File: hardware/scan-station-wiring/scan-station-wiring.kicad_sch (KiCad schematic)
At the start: 66 parts, among them J10 Buttons/Encoder, J11 GPIO Expansion, J1A CYD Expansion (SPI2), J1B CYD UART (PWR+HS), J2 NFC Antenna A, J3 RGB LED Header, J4 NFC Antenna B, J5 USB-C, J6 Load Cell, J7 CAN Bus, J8 I2C1 Expansion, J9 TOF Sensor (I2C1), Q1 TVDD_SW_A, Q2 TVDD_SW_B, Q3 BSS138 (SDA), Q4 BSS138 (SCL), SW1 RESET, SW2 BOOT, U1 ESP32-S3-WROOM-1, U2 ADS1220IPWR, U3 AHT20, U4 PN5180A0HN, U5 AS7341-DLGM, U6 AMS1117-3.3, U7 SN65HVD230DR, U8 AMS1117-1.8, Y1 27.12MHz

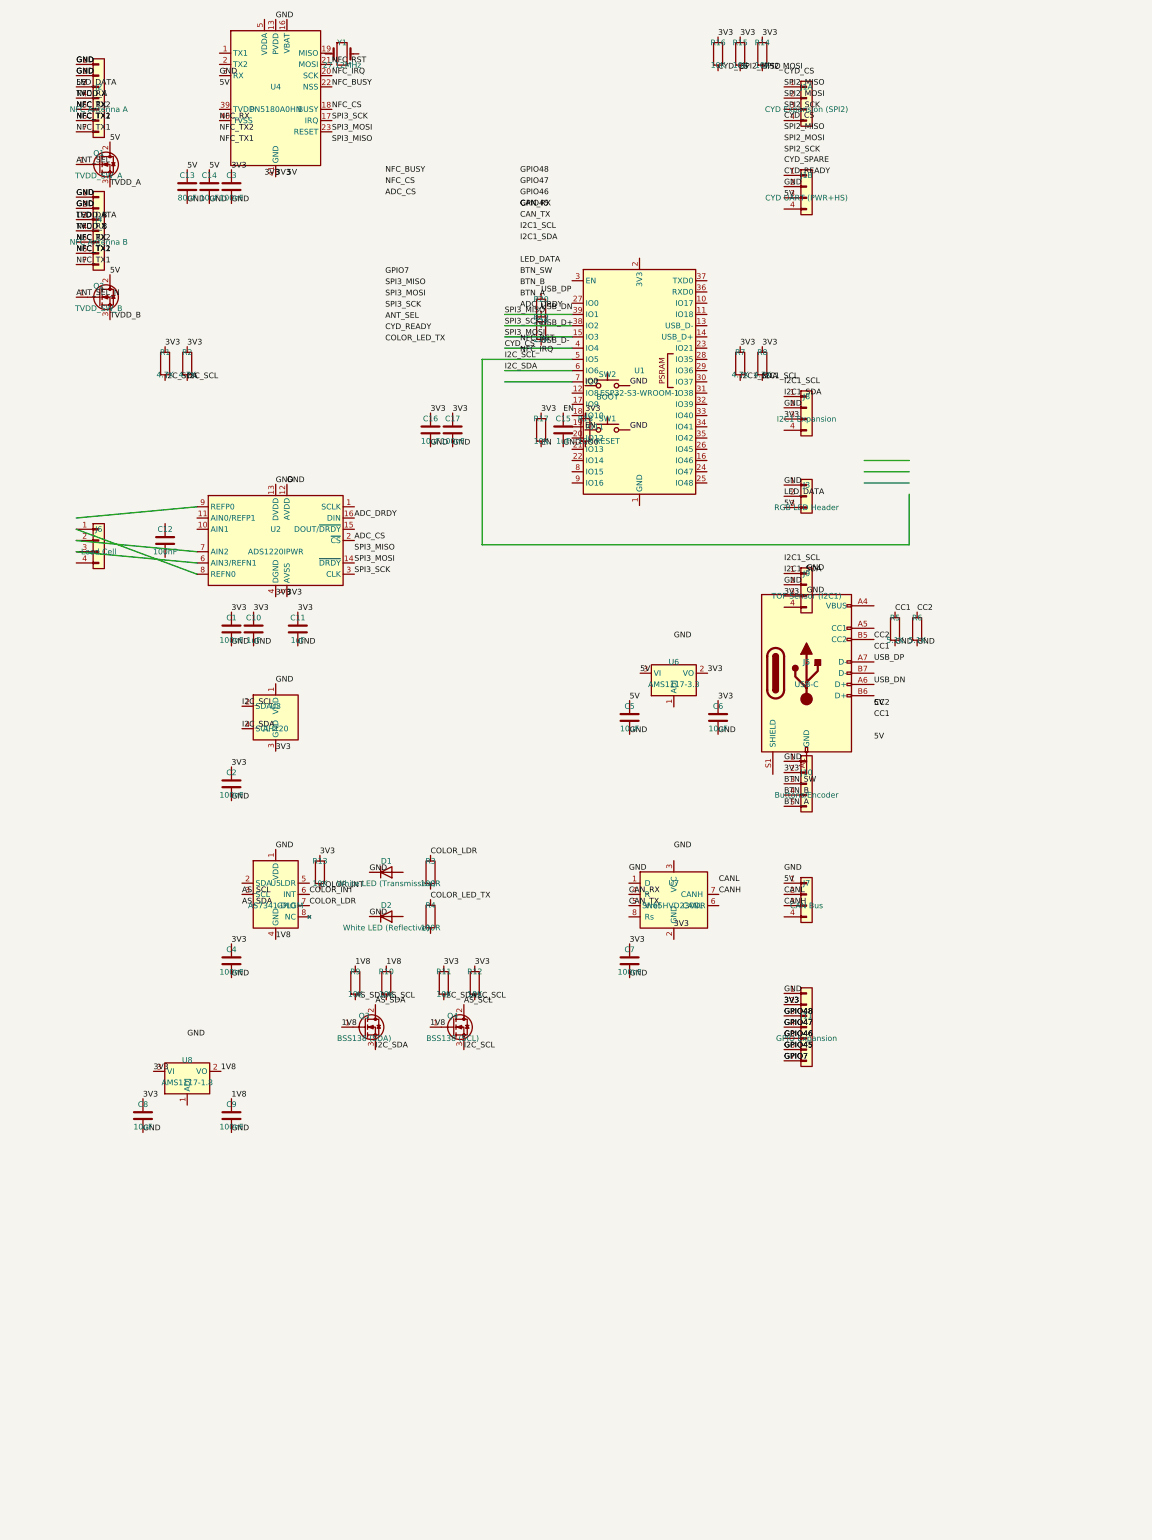
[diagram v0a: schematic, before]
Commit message: feat: add dual USB, CH340C, W5500 Ethernet, PoE header
Major additions:
- CH340C USB-to-UART (U9) for programming via J5 USB-C (IO43/IO44)
- USB OTG host port (J12 USB-C) on IO19/IO20 for label printers
- W5500 Ethernet controller (U10) on SPI3 bus with RJ45 MagJack (J13)
- PoE module headers: J14 (48V input from RJ45) + J15 (5V output)
  Compatible with off-the-shelf PoE PD modules
- Reset button (SW1) + Boot button (SW2) for bare WROOM module
- CYD connector GPIOs corrected (carrier IO7/IO45, not CYD IO43/44)

All 41 ESP32-S3 GPIOs now assigned. Full pin map:
- SPI2 (IO10-13): CYD display
- SPI3 (IO4-6): ADS1220 + PN5180 + W5500
- I2C0 (IO8-9): AHT20 + AS7341
- I2C1 (IO39-40): TOF + expansion
- CAN (IO41-42): SN65HVD230
- UART (IO43-44): CH340C programming
- USB OTG (IO19-20): Host mode
- ETH (IO46-48): W5500 CS/INT/RST
- NFC (IO14-18): PN5180 CS/BUSY/IRQ/RST
- Misc: LED_DATA(38), ANT_SEL(3), buttons(35-37), color(1,7)

Co-Authored-By: Claude Opus 4.6 (1M context) <noreply@anthropic.com>
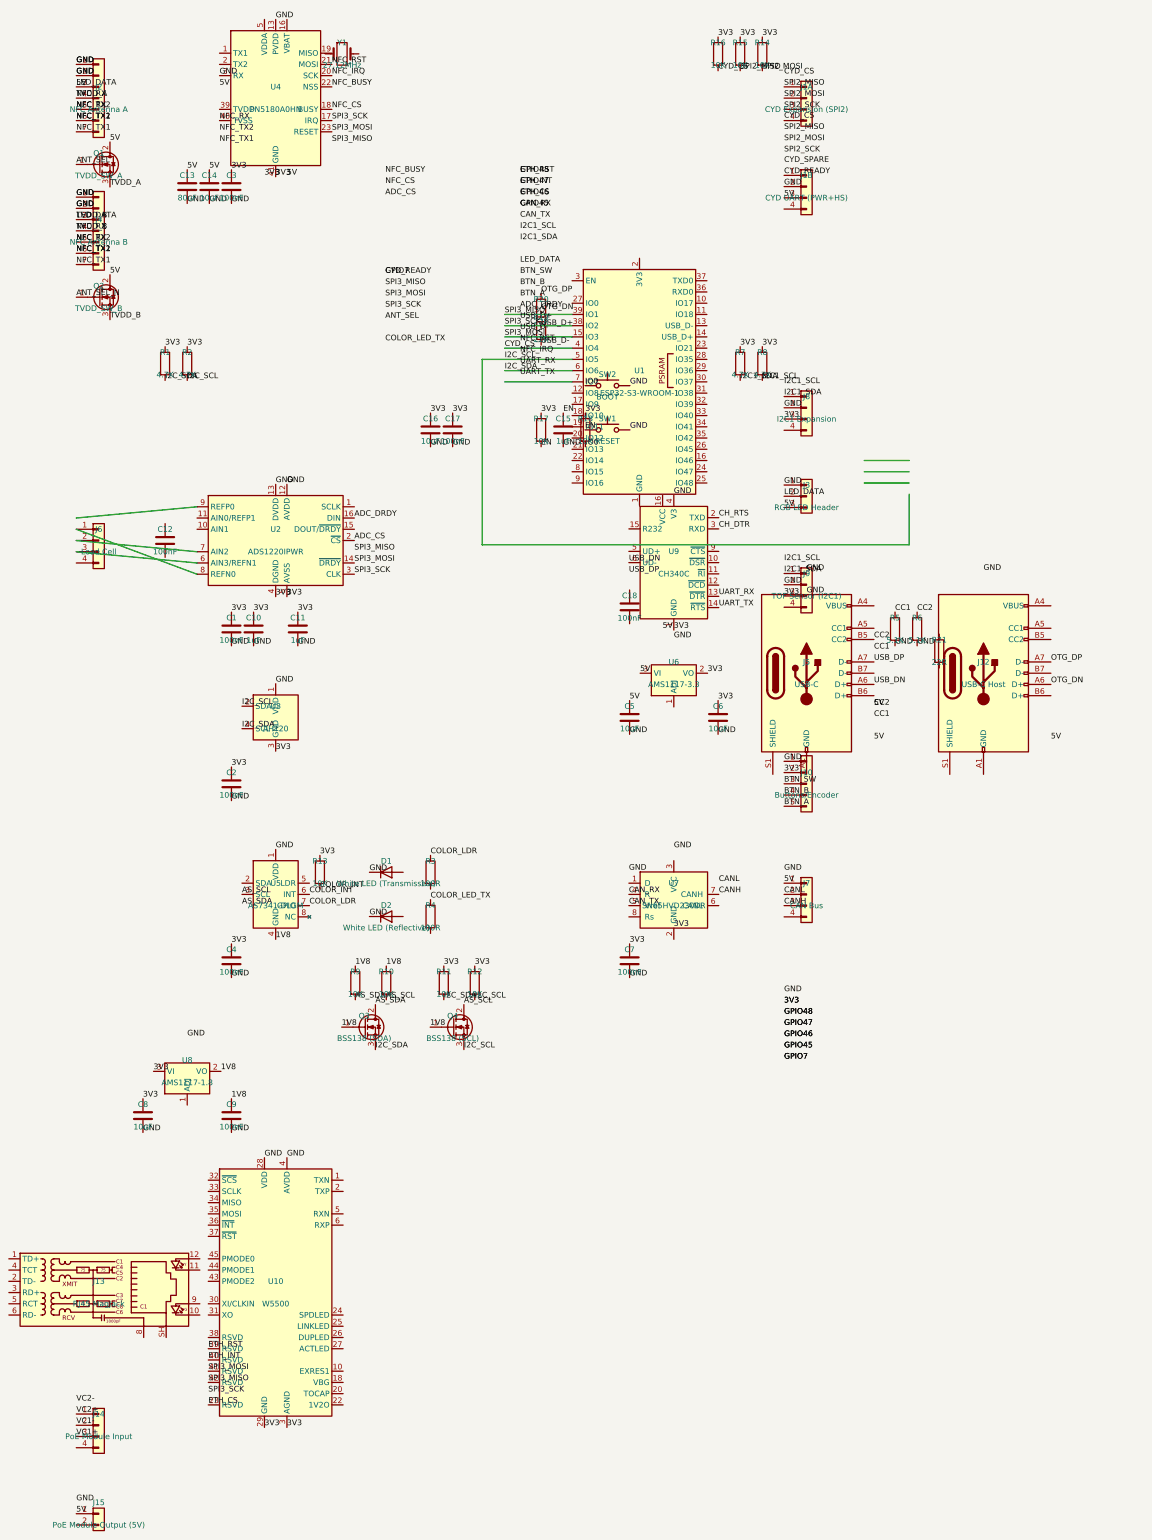
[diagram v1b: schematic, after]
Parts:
- removed J11: GPIO Expansion, symbol Connector_Generic:Conn_01x07
- added C18: 100nF, symbol Device:C
- added J12: USB-C Host, symbol Connector:USB_C_Receptacle_USB2.0_14P
- added J13: RJ45 MagJack, symbol Connector:RJ45_Hanrun_HR911105A_Horizontal
- added J14: PoE Module Input, symbol Connector_Generic:Conn_01x04
- added J15: PoE Module Output (5V), symbol Connector_Generic:Conn_01x02
- added R21: 22R, symbol Device:R
- added U10: W5500, symbol Interface_Ethernet:W5500
- added U9: CH340C, symbol Interface_USB:CH340C
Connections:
- net 3V3: now also U10.14 (AGND), U10.16 (AGND), U10.19 (AGND), U10.29 (GND), U10.3 (AGND), U10.48 (AGND), U10.9 (AGND), U9.1 (GND)
- net 5V: now also J15.1 (Pin_1)
- net GND: now also U10.11 (AVDD), U10.15 (AVDD), U10.17 (AVDD), U10.21 (AVDD), U10.28 (VDD), U10.4 (AVDD), U10.8 (AVDD), U9.4 (V3)
- net SPI3_MISO: now also U10.42 (RSVD)
- net SPI3_MOSI: now also U10.41 (RSVD)
- net USB_DN: now also U9.6 (UD-); no longer R19.1
- net USB_DP: no longer R20.1
- new net: J12.A1 (GND), J12.A12 (GND), J12.B1 (GND), J12.B12 (GND)
- new net: J12.A4 (VBUS), J12.A9 (VBUS), J12.B4 (VBUS), J12.B9 (VBUS)
- new net CH_DTR: U9.3 (RXD)
- new net CH_RTS: U9.2 (TXD)
- new net ETH_CS: U10.23 (RSVD)
- new net ETH_INT: U10.40 (RSVD)
- new net ETH_RST: U10.39 (RSVD)
- new net OTG_DN: J12.A6 (D+), R19.1
- new net OTG_DP: J12.A7 (D-), R20.1
- new net UART_RX: U9.13 (~{DTR})
- new net UART_TX: U9.14 (~{RTS})
- new net VC1+: J14.3 (Pin_3)
- new net VC1-: J14.2 (Pin_2)
- new net VC2+: J14.1 (Pin_1)

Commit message: feat: second load cell, touch buttons, auto-reset, ETH LEDs, PSRAM
- Second load cell connector (J16) on ADS1220 AIN2/AIN3 for FillaShelf
- Move buttons to touch-capable pins (IO1/IO2/IO7 → BTN_SW/A/B)
  Non-touch functions (CYD_READY, CYD_SPARE, COLOR_LED_TX) to IO35-37
- CH340C auto-reset circuit: DTR→EN, RTS→IO0 via 100nF caps (C19/C20)
- W5500 LED outputs wired to RJ45 MagJack (LINKLED, ACTLED)
- W5500 TX/RX pairs connected to RJ45 MagJack
- ESP32-S3-WROOM-1-N16R8 (16MB flash + 8MB PSRAM) specified

Updated GPIO map:
- IO1 → BTN_SW (touch capable)
- IO2 → BTN_A (touch capable)
- IO7 → BTN_B (touch capable)
- IO35 → CYD_READY
- IO36 → CYD_SPARE
- IO37 → COLOR_LED_TX

Co-Authored-By: Claude Opus 4.6 (1M context) <noreply@anthropic.com>
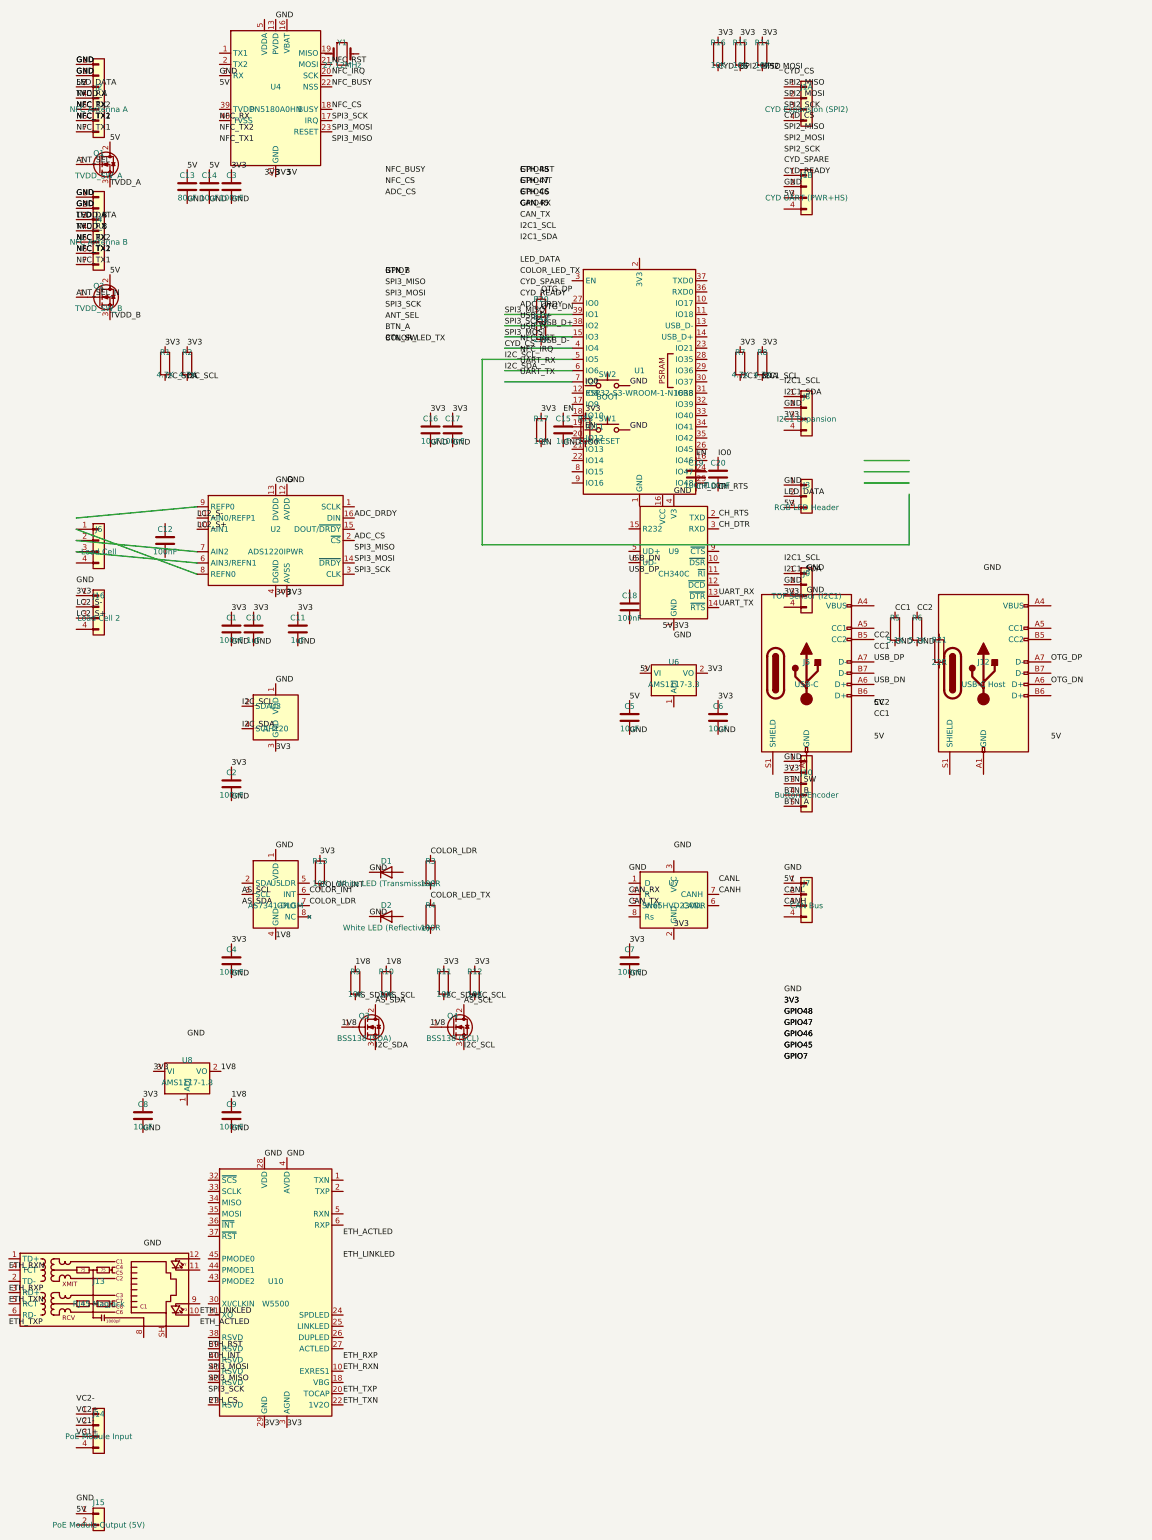
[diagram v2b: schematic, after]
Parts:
- added C19, C20: 100nF, symbol Device:C
- added J16: Load Cell 2, symbol Connector_Generic:Conn_01x04
- U1: value ESP32-S3-WROOM-1 -> ESP32-S3-WROOM-1-N16R8
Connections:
- net COLOR_LED_TX is gone; now on net BTN_SW: R4.1
- net 3V3: now also J16.1 (Pin_1)
- net CH_DTR: now also C19.2
- net CH_RTS: now also C20.2
- net EN: now also C19.1
- net IO0: now also C20.1
- net ETH_RXN: now reaches U10.10 (EXRES1)
- net ETH_RXN: now also J13.4 (TCT)
- net ETH_TXP: now reaches U10.20 (TOCAP)
- net ETH_TXN: now reaches U10.22 (1V2O)
- net ETH_TXN: now also J13.5 (RCT)
- net LC2_S+: now reaches U2.10 (AIN1)
- net LC2_S+: now also J16.3 (Pin_3)
- net LC2_S-: now reaches U2.11 (AIN0/REFP1)
- net LC2_S-: now also J16.2 (Pin_2)
- net ETH_LINKLED: now reaches J13.10
- net ETH_RXP: now reaches J13.3 (RD+)

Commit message: chore: second schematic cleanup pass
- Remove 22 orphaned labels (GPIO expansion, duplicates, stale pins)
- Pretty-print .kicad_sch (was single line again after MCP edits)
- Fix CYD_SPARE label on ESP32 IO36
- Remove old COLOR_LED_TX from IO1 (moved to IO37)
- Remove GPIO7/45/46/47/48 expansion labels (J11 deleted)
- Remove duplicate GND/3V3 labels at old antenna connector positions

Co-Authored-By: Claude Opus 4.6 (1M context) <noreply@anthropic.com>
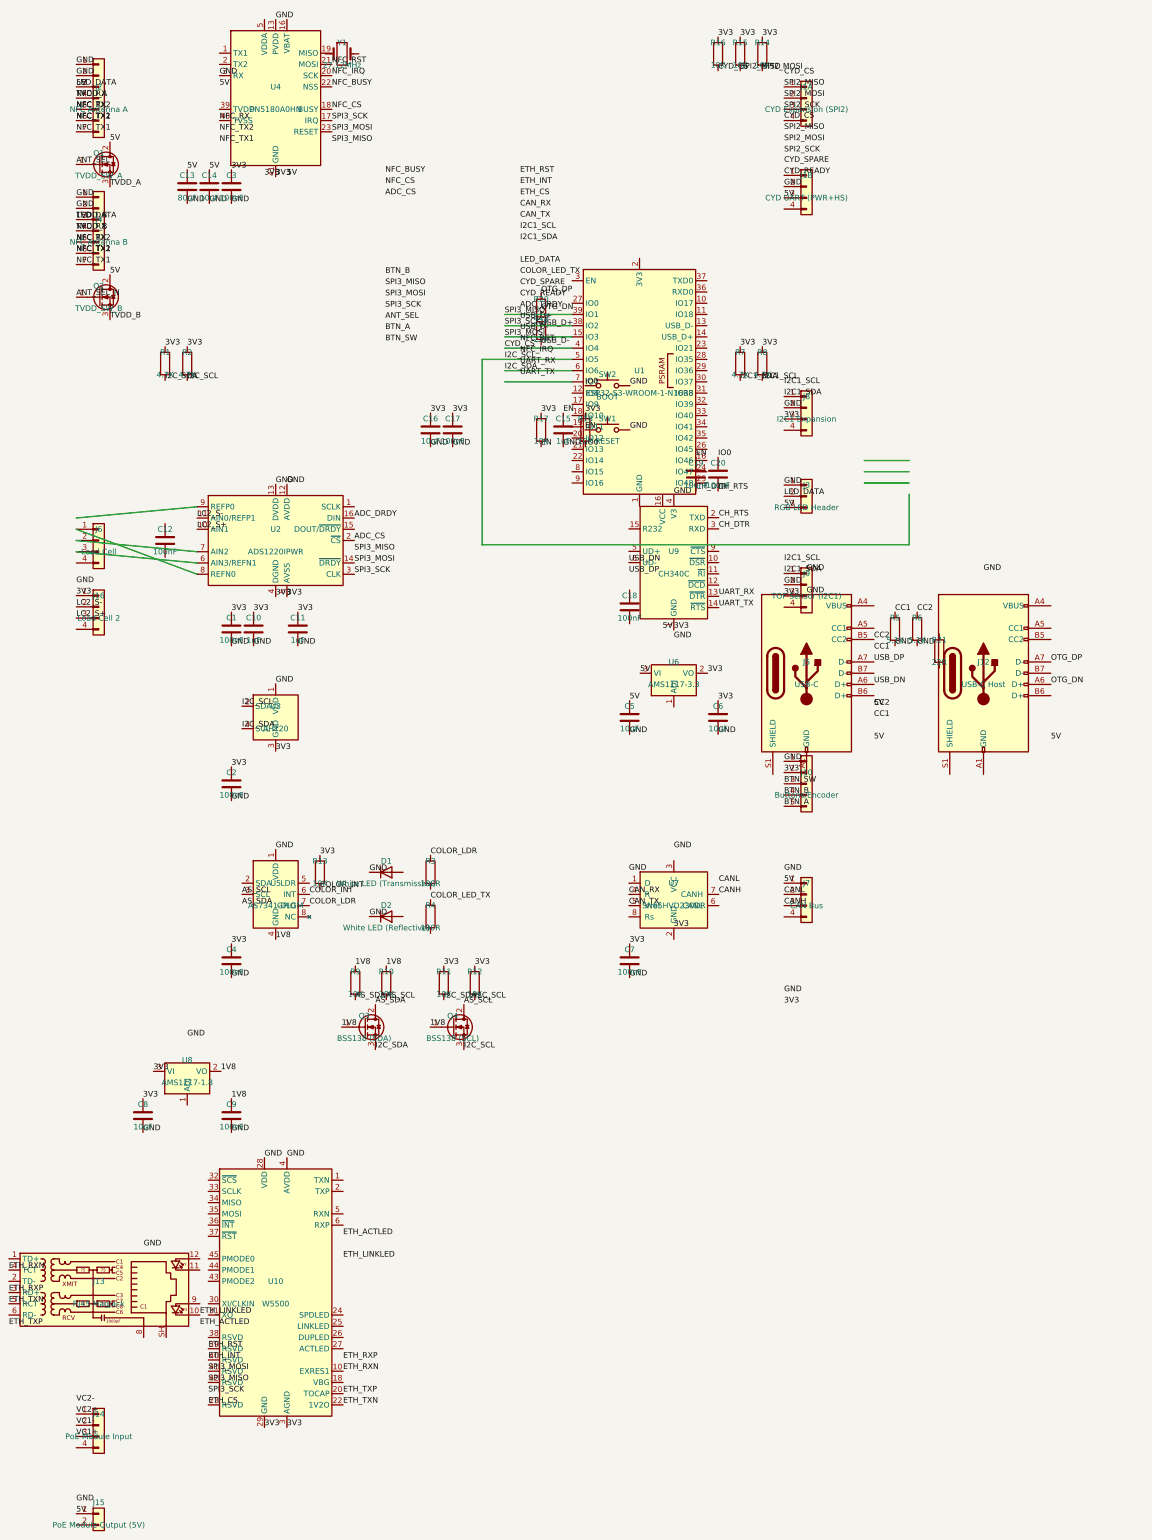
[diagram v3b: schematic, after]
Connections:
- net BTN_SW: no longer R4.1
- new net COLOR_LED_TX: R4.1

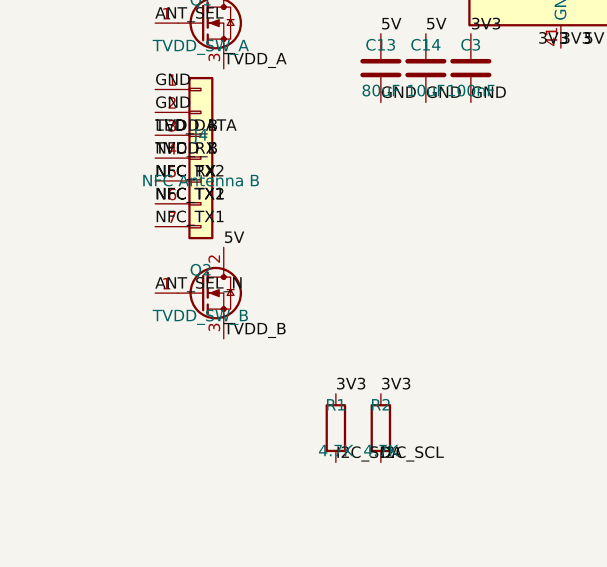
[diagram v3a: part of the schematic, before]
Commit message: fix: swap Q2 to P-MOSFET for antenna switching, remove ANT_SEL_N
Q1 (N-MOS) and Q2 (P-MOS) now share the same ANT_SEL GPIO:
- ANT_SEL HIGH: Q1 on (antenna A), Q2 off (antenna B)
- ANT_SEL LOW: Q1 off (antenna A), Q2 on (antenna B)

Eliminates need for inverter or second GPIO. ERC passes clean.

Co-Authored-By: Claude Opus 4.6 (1M context) <noreply@anthropic.com>
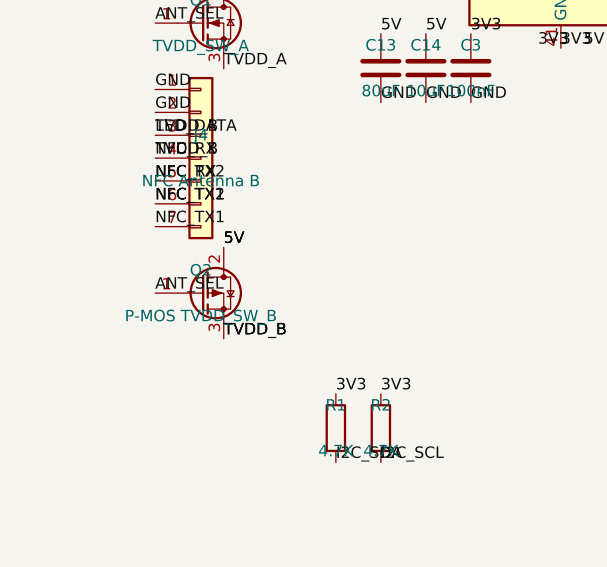
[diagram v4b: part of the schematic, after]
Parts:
- removed Q2: TVDD_SW_B, symbol Transistor_FET:Q_NMOS_GDS
- added Q2: P-MOS TVDD_SW_B, symbol Transistor_FET:Q_PMOS_GDS
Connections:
- net 5V: now also Q2.2 (D), Q2.3 (S)
- net ANT_SEL: now also Q2.1 (G)
